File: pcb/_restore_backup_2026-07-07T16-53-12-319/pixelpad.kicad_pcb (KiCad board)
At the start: 2 copper layers, 16 parts, among them J1 OLED Display, SW1 SW_Push_45deg, SW2 SW_Push_45deg, SW3 RotaryEncoder_Switch, SW4 SW_Push_45deg, SW5 SW_Push_45deg, SW6 SW_Push_45deg, U1 MOUDLE-SEEEDUINO-XIAO

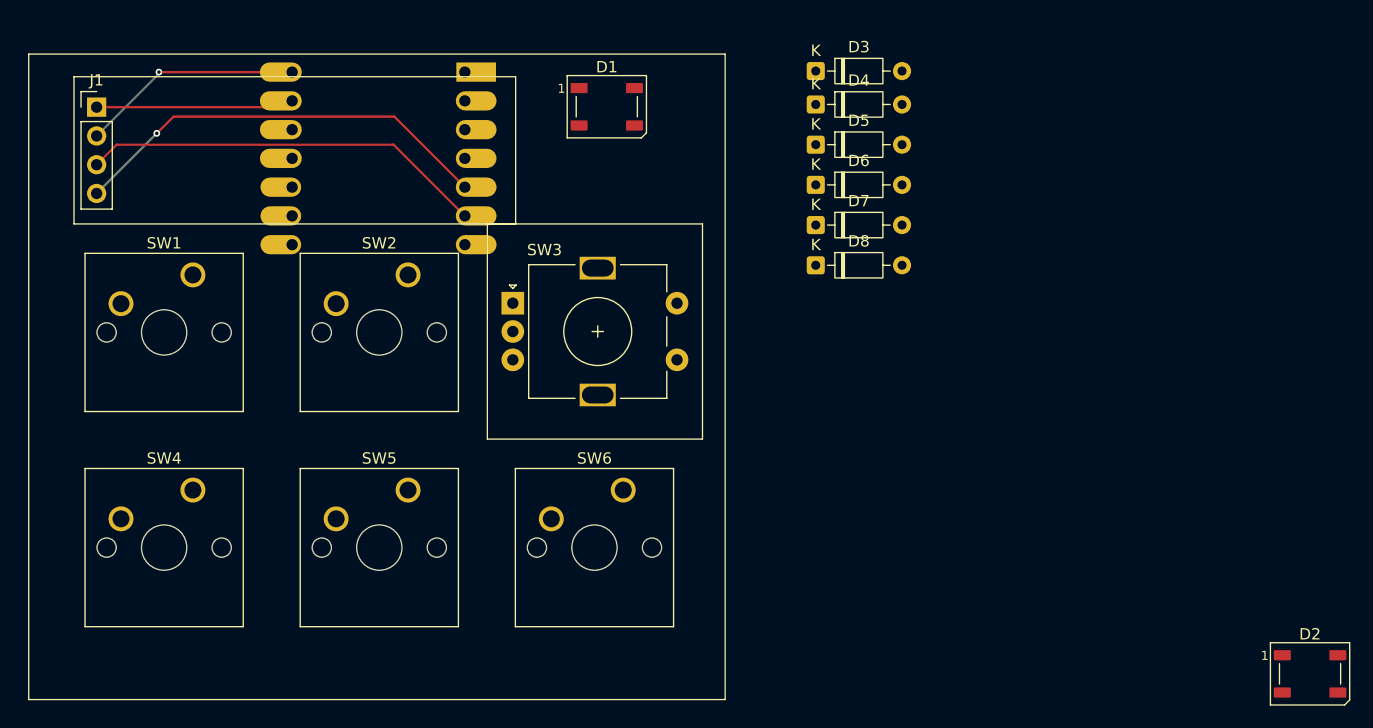
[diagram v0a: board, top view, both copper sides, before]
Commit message: Made the rectangle to show where the oled would be
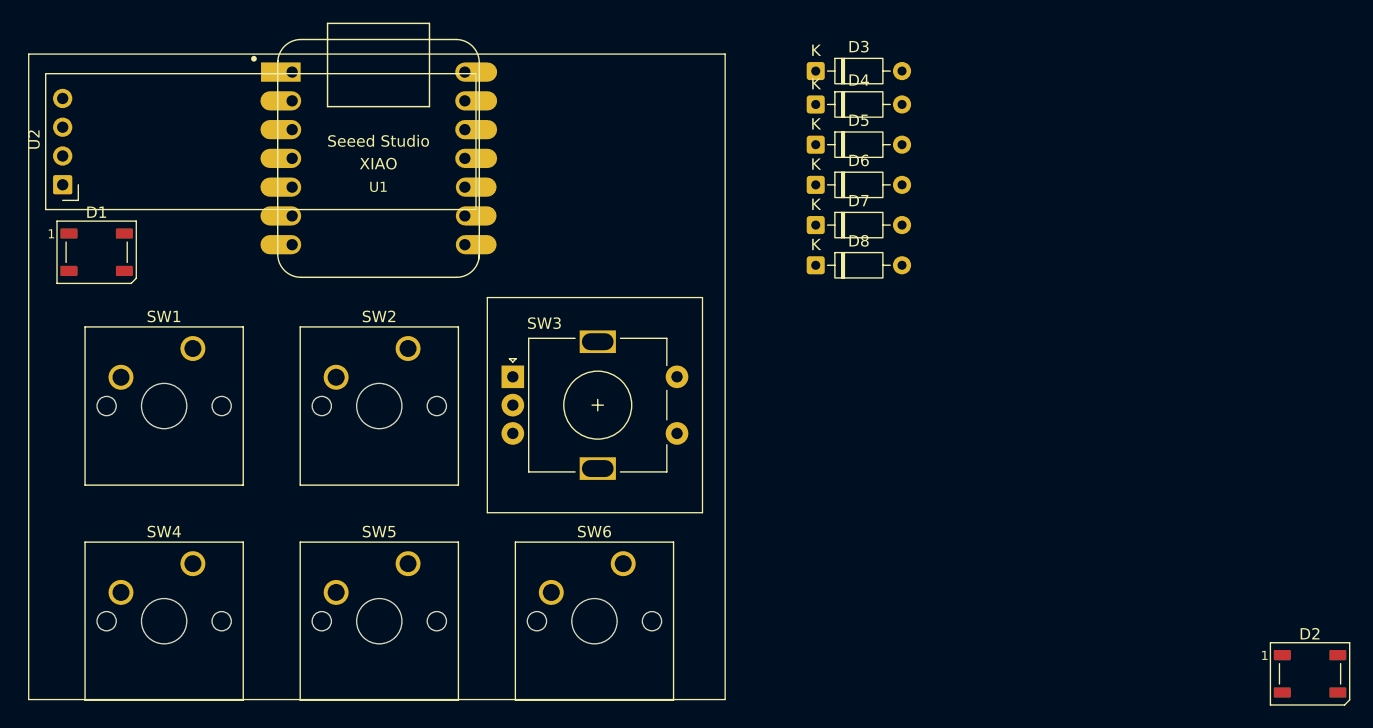
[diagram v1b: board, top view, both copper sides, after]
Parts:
- removed J1: OLED Display, Connector_PinHeader_2.54mm:PinHeader_1x04_P2.54mm_Vertical
- added U2: ER_OLEDM0.91_1x-I2C, Display:ER_OLEDM0.91_1x-I2C, F.Cu at (58.5, 46.0)
- U1: moved to F.Cu
- moved D1 46.8 mm to (61.5, 52.0)
- moved SW1 6.50 mm to (70.0, 60.5)
- moved SW2 6.50 mm to (89.0, 60.5)
- moved SW3 6.50 mm to (98.2, 63.0)
- moved SW4 6.50 mm to (70.0, 79.5)
- moved SW5 6.50 mm to (89.0, 79.5)
- moved SW6 6.50 mm to (108.0, 79.5)
- turned U1 to 0 degrees
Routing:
- net SDA: track 37.9 -> 0.00 mm, vias 1 -> 0
- net SCL: track 35.9 -> 0.00 mm
- net VCC: track 19.7 -> 0.00 mm, vias 1 -> 0
- net GND: track 17.5 -> 0.00 mm
